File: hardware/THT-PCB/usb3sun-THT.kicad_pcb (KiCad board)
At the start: 2 copper layers, 52 parts, among them J2 8918-P8B, J3 USB-U267-BWS, Q1 2N7002DW, Q3 2N7002DW, Q4 MMBT2222A, Q5 MMBT2222A, Q7 2N7002DW, SW1 TS-1187A-B-A-B, U1 Pico, U2 SRV05-4, U3 SRV05-4, U4 MAX40200AUK, U5 MAX40200AUK

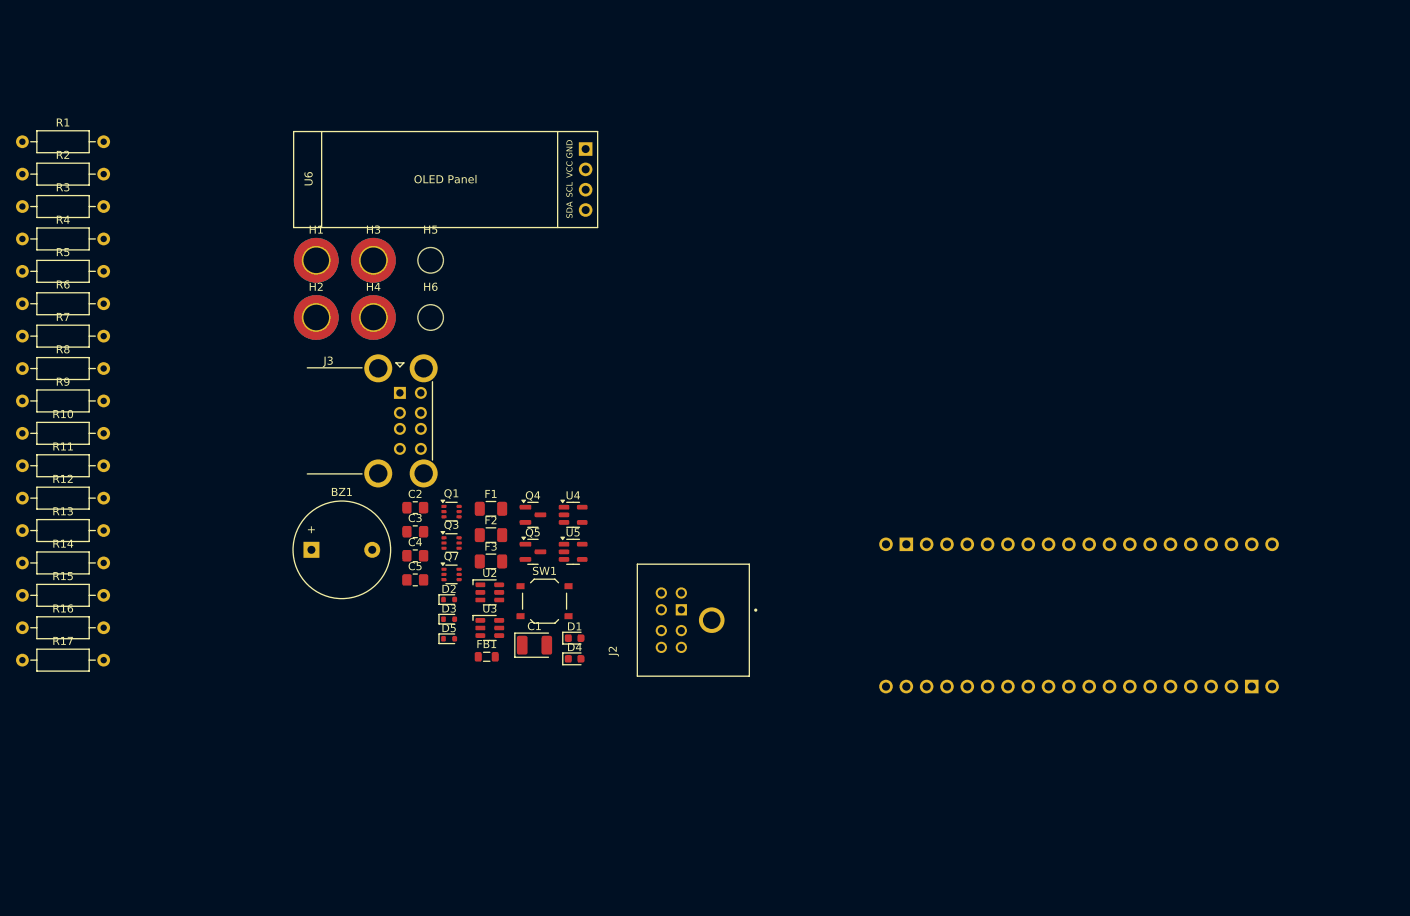
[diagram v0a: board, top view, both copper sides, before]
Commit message: Complete PCB layout, Further schematic adjustments; TODO traces
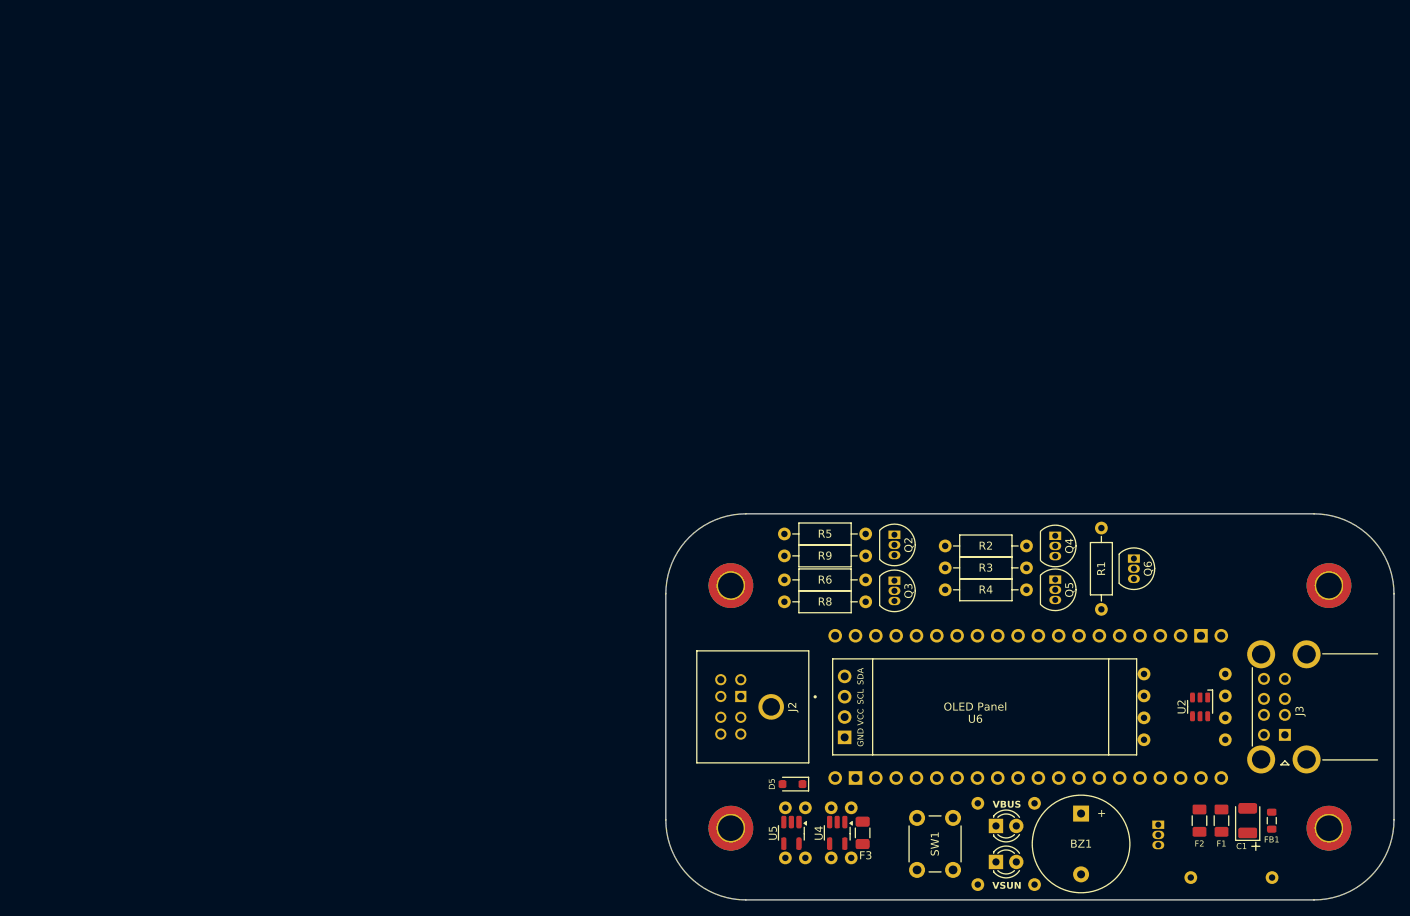
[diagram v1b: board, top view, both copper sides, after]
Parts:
- removed D2, D3: CMOZ1L8, Diode_SMD:D_SOD-523
- removed H5, H6: MountingHole, MountingHole:MountingHole_3.2mm_M3_DIN965
- removed Q7: 2N7002DW, Package_TO_SOT_SMD:SOT-363_SC-70-6
- removed R16: 1kΩ, Resistor_THT:R_Axial_DIN0207_L6.3mm_D2.5mm_P10.16mm_Horizontal
- removed R17: 6k2Ω, Resistor_THT:R_Axial_DIN0207_L6.3mm_D2.5mm_P10.16mm_Horizontal
- removed U3: SRV05-4, marbastlib-various:SOT-23-6-routable
- added Q2: 2N7000, Package_TO_SOT_THT:TO-92_Inline, F.Cu at (148.4, 100.4)
- added Q6: 2N7000, Package_TO_SOT_THT:TO-92_Inline, F.Cu at (178.3, 103.4)
- C2, C3, C4, C5: footprint Capacitor_SMD:C_0805_2012Metric_Pad1.18x1.45mm_HandSolder -> Capacitor_THT:C_Disc_D3.8mm_W2.6mm_P2.50mm; moved to B.Cu
- D1, D4: value 19-213/Y2C-CQ2R2L/3T(CY) -> ~; footprint LED_SMD:LED_0603_1608Metric -> LED_THT:LED_D3.0mm
- D5: value ESD5Z5V0 -> SDD32C05L01; footprint Diode_SMD:D_SOD-523 -> Diode_SMD:D_SOD-323_HandSoldering
- Q1: value 2N7002DW -> 2N7000; footprint Package_TO_SOT_SMD:SOT-363_SC-70-6 -> Package_TO_SOT_THT:TO-92_Inline; moved to B.Cu
- Q3: value 2N7002DW -> 2N7000; footprint Package_TO_SOT_SMD:SOT-363_SC-70-6 -> Package_TO_SOT_THT:TO-92_Inline
- Q4, Q5: value MMBT2222A -> 2N7000; footprint Package_TO_SOT_SMD:SOT-23 -> Package_TO_SOT_THT:TO-92_Inline
- R10, R11, R12, R13, R15, R7, U1: moved to B.Cu
- R14: value 6k2Ω -> 1kΩ; moved to B.Cu
- SW1: value TS-1187A-B-A-B -> TS665CJ; footprint Button_Switch_SMD:SW_Push_1P1T_XKB_TS-1187A -> Button_Switch_THT:SW_PUSH_6mm_H4.3mm
- U4, U5: footprint Package_TO_SOT_SMD:SOT-23-5 -> Package_TO_SOT_SMD:SOT-23-5_HandSoldering
- moved R7 161.0 mm to (185.4, 143.3)
- moved R10 153.9 mm to (189.7, 120.6), turned to 180 degrees
- moved R12 152.8 mm to (189.7, 123.3), turned to 180 degrees
- moved R13 152.6 mm to (189.7, 126.0), turned to 180 degrees
- moved R11 152.6 mm to (189.7, 117.8), turned to 180 degrees
- moved R1 143.3 mm to (174.2, 99.6), turned to -90 degrees
- moved H2 141.8 mm to (202.7, 137.1)
- moved H1 133.0 mm to (202.7, 106.8)
- moved R14 132.8 mm to (165.9, 144.1), turned to 90 degrees
- moved U6 131.1 mm to (178.7, 127.9), turned to 180 degrees
- moved R2 124.4 mm to (154.7, 101.8)
- moved R3 123.9 mm to (154.7, 104.5)
- moved R4 123.4 mm to (154.7, 107.3)
- moved R15 122.2 mm to (158.8, 134.0), turned to -90 degrees
- moved J3 118.6 mm to (197.2, 125.4), turned to 180 degrees
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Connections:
- H1 pad 1: GNDPWR -> unconnected-(H1-Pad1)_1
- Q1 pad 1: /INT_KTX -> GND
- Q1 pad 2: +3V3 -> /INT_SPOWER
- Q1 pad 3: /KRX -> /SPOWER
- Q3 pad 1: GND -> /INT_MTX
- Q3 pad 2: /INT_SPOWER -> +3V3
- Q4 pad 1: Net-(D2-K) -> /INT_KTX
- Q4 pad 2: Net-(Q4-E) -> +3V3
- Q4 pad 3: Net-(D1-K) -> /KTX
- Q5 pad 1: Net-(D3-K) -> GND
- Q5 pad 2: Net-(Q5-E) -> /KTX_ENABLE#
- Q5 pad 3: Net-(D4-K) -> /INT_KTX
- R14 pad 1: Net-(Q4-E) -> Net-(D4-K)
- R15 pad 1: VBUS -> Net-(D1-K)
- R15 pad 2: Net-(D2-K) -> GND
- U1 pad 40: unconnected-(U1-VBUS-Pad40) -> VBUS
- U2 pad 1: /D2- -> /D2+
- U2 pad 3: unconnected-(U2-IO2-Pad3) -> /D2-
- U2 pad 4: unconnected-(U2-IO3-Pad4) -> /D1-
- U2 pad 6: /D2+ -> /D1+
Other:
- board outline added: 91 x 48.3 mm
- board text added: "VBUS"
- board text added: "VSUN"

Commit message: Fully Routed
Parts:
- Q2, Q3, Q6, R1, R5, R6, R8, R9: moved to B.Cu
- moved R3 97.7 mm to (74.9, 48.2)
- moved R7 93.0 mm to (117.1, 80.2)
- moved Q1 90.7 mm to (117.3, 72.4), turned to 0 degrees
- moved R14 88.1 mm to (104.2, 81.2)
- moved R15 88.1 mm to (97.1, 71.1)
- moved C1 87.5 mm to (130.8, 74.1)
- moved D1 87.5 mm to (99.3, 74.8)
- moved D4 87.5 mm to (99.3, 79.3)
- moved H2 87.5 mm to (141.0, 75.1)
- moved H3 87.5 mm to (66.2, 44.7)
- moved H4 87.5 mm to (66.2, 75.1)
- moved J2 87.5 mm to (75.9, 59.9)
- moved U6 87.5 mm to (116.9, 65.9)
- moved D5 87.5 mm to (73.9, 69.6)
- moved F1 87.5 mm to (127.5, 74.1)
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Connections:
- R10 pad 1: /D2+ -> /D1+
- R10 pad 2: /INT_D2+ -> /INT_D1+
- R11 pad 1: /D2- -> /D2+
- R11 pad 2: /INT_D2- -> /INT_D2+
- R12 pad 1: /D1+ -> /D1-
- R12 pad 2: /INT_D1+ -> /INT_D1-
- R13 pad 1: /D1- -> /D2-
- R13 pad 2: /INT_D1- -> /INT_D2-
- U2 pad 1: /D2+ -> /D1+
- U2 pad 3: /D2- -> /D2+
- U2 pad 4: /D1- -> /D2-
- U2 pad 6: /D1+ -> /D1-
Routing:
- net VSUN: track 0.00 -> 107.5 mm
- net +3V3: track 0.00 -> 88.8 mm
- net +5V: track 0.00 -> 78.8 mm, vias 0 -> 3
- net /SPOWER: track 0.00 -> 73.5 mm, vias 0 -> 1
- net /KTX: track 0.00 -> 54.7 mm
- net /DISPLAY_SDA: track 0.00 -> 54.1 mm, vias 0 -> 1
- net /DISPLAY_SCL: track 0.00 -> 50.8 mm, vias 0 -> 1
- net /MTX: track 0.00 -> 43.9 mm
- net /KRX: track 0.00 -> 41.5 mm, vias 0 -> 1
- net /INT_D2-: track 0.00 -> 37.5 mm
- net /INT_KTX: track 0.00 -> 35.6 mm
- net /INT_MTX: track 0.00 -> 35.1 mm, vias 0 -> 1
- net /DISPLAY_GND: track 0.00 -> 34.5 mm, vias 0 -> 2
- net /INT_D2+: track 0.00 -> 34.0 mm, vias 0 -> 1
- net /INT_SPOWER: track 0.00 -> 33.5 mm
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- added copper zone on B.Cu, net GND
- added copper zone on F.Cu, net GND
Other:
- board size 91 x 48.3 mm -> 91 x 43.8 mm

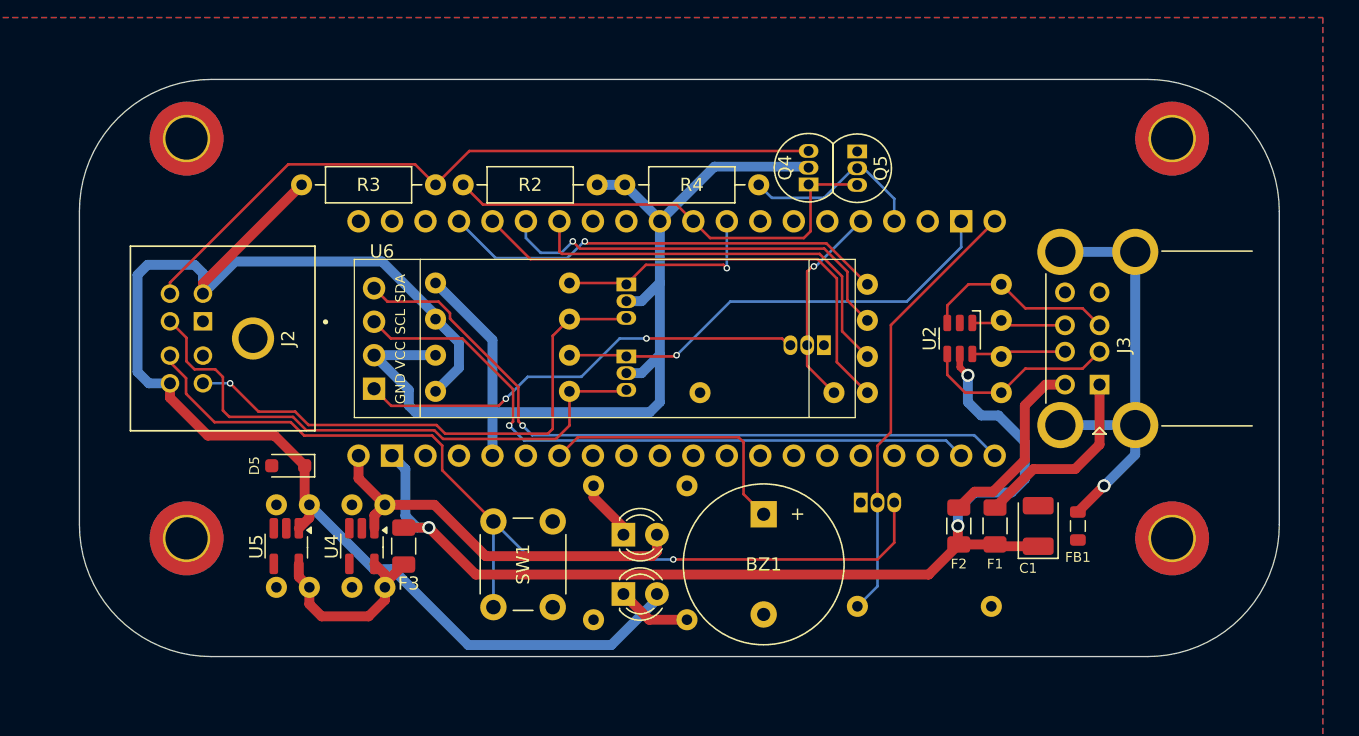
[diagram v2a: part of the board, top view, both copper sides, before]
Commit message: Cleanup, Footprint location reshuffling
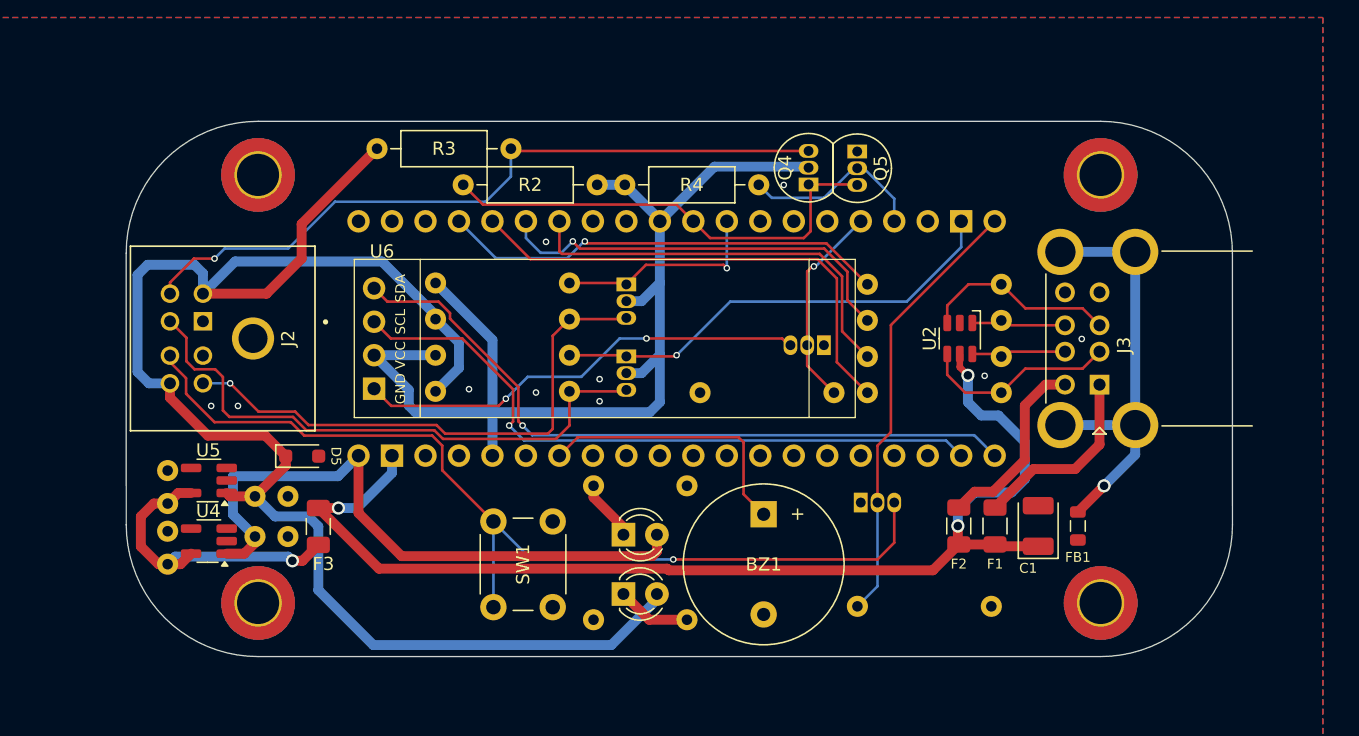
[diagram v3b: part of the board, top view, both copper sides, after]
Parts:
- moved C4 16.6 mm to (64.8, 77.0), turned to 90 degrees
- moved C5 12.5 mm to (64.8, 72.4), turned to 90 degrees
- moved U4 11.6 mm to (67.9, 75.3), turned to 180 degrees
- moved C2 10.1 mm to (71.4, 74.9), turned to 0 degrees
- moved U5 7.70 mm to (67.9, 70.7), turned to 180 degrees
- moved H2 7.31 mm to (135.5, 80.0)
- moved H4 7.31 mm to (71.6, 80.0)
- moved F3 6.65 mm to (76.2, 74.2)
- moved R3 6.34 mm to (80.7, 45.5)
- moved H1 6.09 mm to (135.5, 47.5)
- moved H3 6.08 mm to (71.6, 47.5)
- moved C3 4.18 mm to (71.4, 71.9), turned to 0 degrees
- moved D5 1.29 mm to (75.0, 68.8), turned to 0 degrees
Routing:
- net VBUS: track 30.3 -> 48.2 mm
- net VSUN: track 107.5 -> 122.0 mm
- net /VRAW: track 15.4 -> 23.8 mm, vias 0 -> 1
- net +5V: track 78.8 -> 86.5 mm
- net /KTX: track 54.7 -> 54.8 mm, vias 0 -> 1
- net GND: vias 0 -> 10
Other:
- board size 91 x 43.8 mm -> 83.9 x 40.6 mm
